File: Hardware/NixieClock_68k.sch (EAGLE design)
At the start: 56 parts, among them IC1 68008, IC10 7805, IC11 MIC803, IC12 74HC08N, IC2 AS6C1008, IC3 39SF020, IC4 DS1244Y, IC5 68681, IC6 74HC30N, IC7 74HC04N, IC8 74HC138N, IC9 74HC266N, Q1 4MHz, Q2 3.6864MHz

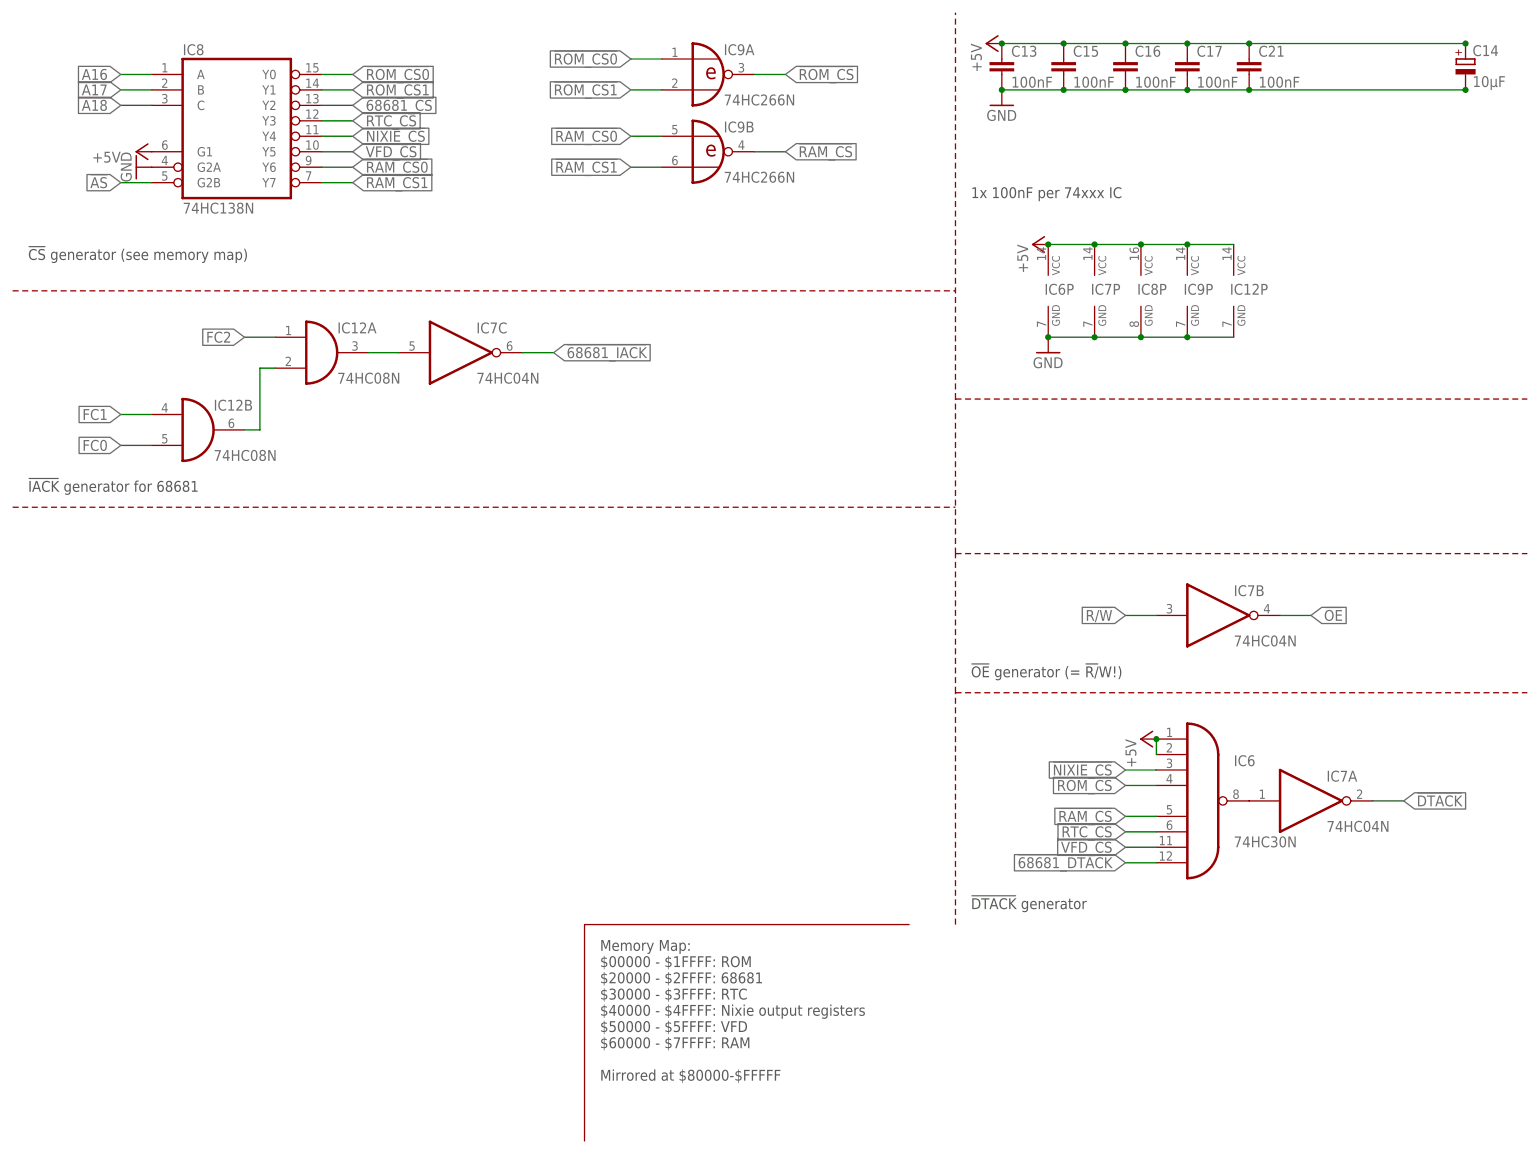
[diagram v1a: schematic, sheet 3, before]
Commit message: routed most system control signals
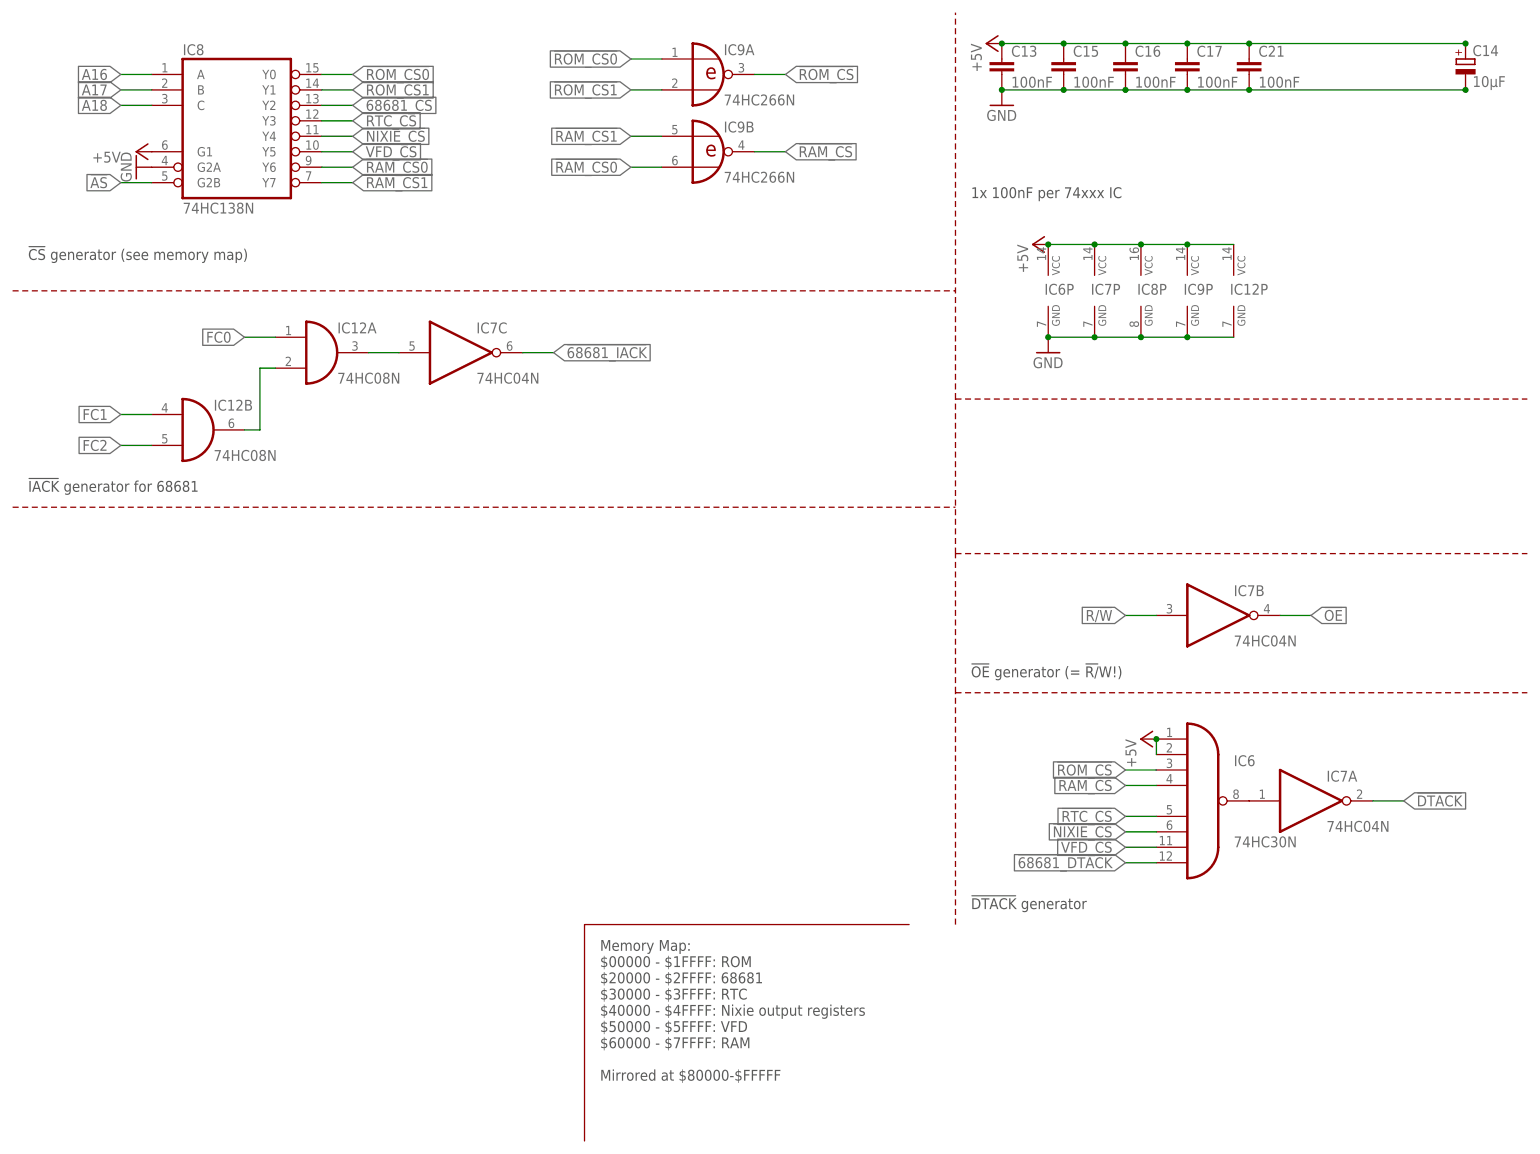
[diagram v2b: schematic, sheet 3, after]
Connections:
- net !NIXIE_CS: now also IC6A.I5; no longer IC6A.I2
- net !RAM_CS: now also IC6A.I3; no longer IC6A.I4
- net !RAM_CS0: now also IC9B.I1; no longer IC9B.I0
- net !RAM_CS1: now also IC9B.I0; no longer IC9B.I1
- net !ROM_CS: now also IC6A.I2; no longer IC6A.I3
- net !RTC_CS: now also IC6A.I4; no longer IC6A.I5
- net FC0: now also IC12A.I0; no longer IC12B.I1
- net FC2: now also IC12B.I1; no longer IC12A.I0
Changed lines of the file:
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@@
 <net name="!RTC_CS" class="0">
+<segment>
+<pinref part="IC8" gate="A" pin="Y3"/>
+<wire x1="50.8" y1="167.64" x2="55.88" y2="167.64" width="0.1524" layer="91"/>
+<label x="55.88" y="167.64" size="1.778" layer="95" xref="yes"/>
+</segment>
+<segment>
+<pinref part="IC6" gate="A" pin="I4"/>
+<wire x1="187.96" y1="53.34" x2="182.88" y2="53.34" width="0.1524" layer="91"/>
+<label x="182.88" y="53.34" size="1.778" layer="95" rot="R180" xref="yes"/>
+</segment>
+</net>
+<net name="!RAM_CS" class="0">
+<segment>
+<pinref part="IC9" gate="B" pin="O"/>
+<wire x1="121.92" y1="162.56" x2="127" y2="162.56" width="0.1524" layer="91"/>
+<label x="127" y="162.56" size="1.778" layer="95" xref="yes"/>
+</segment>
+<segment>
+<pinref part="IC6" gate="A" pin="I3"/>
+<wire x1="187.96" y1="58.42" x2="182.88" y2="58.42" width="0.1524" layer="91"/>
+<label x="182.88" y="58.42" size="1.778" layer="95" rot="R180" xref="yes"/>
+</segment>
+</net>
+<net name="!ROM_CS" class="0">
+<segment>
+<pinref part="IC9" gate="A" pin="O"/>
+<wire x1="121.92" y1="175.26" x2="127" y2="175.26" width="0.1524" layer="91"/>
+<label x="127" y="175.26" size="1.778" layer="95" xref="yes"/>
+</segment>
+<segment>
+<pinref part="IC6" gate="A" pin="I2"/>
+<wire x1="187.96" y1="60.96" x2="182.88" y2="60.96" width="0.1524" layer="91"/>
+<label x="182.88" y="60.96" size="1.778" layer="95" rot="R180" xref="yes"/>
+</segment>
+</net>
+<net name="!NIXIE_CS" class="0">
+<segment>
+<pinref part="IC8" gate="A" pin="Y4"/>
+<wire x1="50.8" y1="165.1" x2="55.88" y2="165.1" width="0.1524" layer="91"/>
+<label x="55.88" y="165.1" size="1.778" layer="95" xref="yes"/>
+</segment>
 <segment>
 <pinref part="IC6" gate="A" pin="I5"/>
@@
 <label x="182.88" y="50.8" size="1.778" layer="95" rot="R180" xref="yes"/>
 </segment>
-<segment>
-<pinref part="IC8" gate="A" pin="Y3"/>
-<wire x1="50.8" y1="167.64" x2="55.88" y2="167.64" width="0.1524" layer="91"/>
-<label x="55.88" y="167.64" size="1.778" layer="95" xref="yes"/>
-</segment>
-</net>
-<net name="!RAM_CS" class="0">
-<segment>
-<pinref part="IC6" gate="A" pin="I4"/>
-<wire x1="187.96" y1="53.34" x2="182.88" y2="53.34" width="0.1524" layer="91"/>
-<label x="182.88" y="53.34" size="1.778" layer="95" rot="R180" xref="yes"/>
-</segment>
-<segment>
-<pinref part="IC9" gate="B" pin="O"/>
-<wire x1="121.92" y1="162.56" x2="127" y2="162.56" width="0.1524" layer="91"/>
-<label x="127" y="162.56" size="1.778" layer="95" xref="yes"/>
-</segment>
-</net>
-<net name="!ROM_CS" class="0">
-<segment>
-<pinref part="IC6" gate="A" pin="I3"/>
-<wire x1="187.96" y1="58.42" x2="182.88" y2="58.42" width="0.1524" layer="91"/>
-<label x="182.88" y="58.42" size="1.778" layer="95" rot="R180" xref="yes"/>
-</segment>
-<segment>
-<pinref part="IC9" gate="A" pin="O"/>
-<wire x1="121.92" y1="175.26" x2="127" y2="175.26" width="0.1524" layer="91"/>
-<label x="127" y="175.26" size="1.778" layer="95" xref="yes"/>
-</segment>
-</net>
-<net name="!NIXIE_CS" class="0">
-<segment>
-<pinref part="IC6" gate="A" pin="I2"/>
-<wire x1="187.96" y1="60.96" x2="182.88" y2="60.96" width="0.1524" layer="91"/>
-<label x="182.88" y="60.96" size="1.778" layer="95" rot="R180" xref="yes"/>
-</segment>
-<segment>
-<pinref part="IC8" gate="A" pin="Y4"/>
-<wire x1="50.8" y1="165.1" x2="55.88" y2="165.1" width="0.1524" layer="91"/>
-<label x="55.88" y="165.1" size="1.778" layer="95" xref="yes"/>
-</segment>
 </net>
 <net name="A18" class="0">
@@
 </segment>
 <segment>
+<pinref part="IC9" gate="B" pin="I1"/>
+<wire x1="106.68" y1="160.02" x2="101.6" y2="160.02" width="0.1524" layer="91"/>
+<label x="101.6" y="160.02" size="1.778" layer="95" rot="R180" xref="yes"/>
+</segment>
+</net>
+<net name="!RAM_CS1" class="0">
+<segment>
+<pinref part="IC8" gate="A" pin="Y7"/>
+<wire x1="50.8" y1="157.48" x2="55.88" y2="157.48" width="0.1524" layer="91"/>
+<label x="55.88" y="157.48" size="1.778" layer="95" xref="yes"/>
+</segment>
+<segment>
 <pinref part="IC9" gate="B" pin="I0"/>
 <wire x1="106.68" y1="165.1" x2="101.6" y2="165.1" width="0.1524" layer="91"/>
@@
 </segment>
 </net>
-<net name="!RAM_CS1" class="0">
-<segment>
-<pinref part="IC8" gate="A" pin="Y7"/>
-<wire x1="50.8" y1="157.48" x2="55.88" y2="157.48" width="0.1524" layer="91"/>
-<label x="55.88" y="157.48" size="1.778" layer="95" xref="yes"/>
-</segment>
-<segment>
-<pinref part="IC9" gate="B" pin="I1"/>
-<wire x1="106.68" y1="160.02" x2="101.6" y2="160.02" width="0.1524" layer="91"/>
-<label x="101.6" y="160.02" size="1.778" layer="95" rot="R180" xref="yes"/>
-</segment>
-</net>
 <net name="!ROM_CS0" class="0">
 <segment>
@@
 <wire x1="58.42" y1="129.54" x2="63.5" y2="129.54" width="0.1524" layer="91"/>
 <pinref part="IC7" gate="C" pin="I"/>
-</segment>
-</net>
-<net name="FC2" class="0">
-<segment>
-<pinref part="IC12" gate="A" pin="I0"/>
-<wire x1="43.18" y1="132.08" x2="38.1" y2="132.08" width="0.1524" layer="91"/>
-<label x="38.1" y="132.08" size="1.778" layer="95" rot="R180" xref="yes"/>
 </segment>
 </net>
@@
 <net name="FC0" class="0">
 <segment>
+<pinref part="IC12" gate="A" pin="I0"/>
+<wire x1="43.18" y1="132.08" x2="38.1" y2="132.08" width="0.1524" layer="91"/>
+<label x="38.1" y="132.08" size="1.778" layer="95" rot="R180" xref="yes"/>
+</segment>
+</net>
+<net name="!68681_IACK" class="0">
+<segment>
+<pinref part="IC7" gate="C" pin="O"/>
+<wire x1="83.82" y1="129.54" x2="88.9" y2="129.54" width="0.1524" layer="91"/>
+<label x="88.9" y="129.54" size="1.778" layer="95" xref="yes"/>
+</segment>
+</net>
+<net name="FC2" class="0">
+<segment>
 <pinref part="IC12" gate="B" pin="I1"/>
 <wire x1="22.86" y1="114.3" x2="17.78" y2="114.3" width="0.1524" layer="91"/>
@@
 </segment>
 </net>
-<net name="!68681_IACK" class="0">
-<segment>
-<pinref part="IC7" gate="C" pin="O"/>
-<wire x1="83.82" y1="129.54" x2="88.9" y2="129.54" width="0.1524" layer="91"/>
-<label x="88.9" y="129.54" size="1.778" layer="95" xref="yes"/>
-</segment>
-</net>

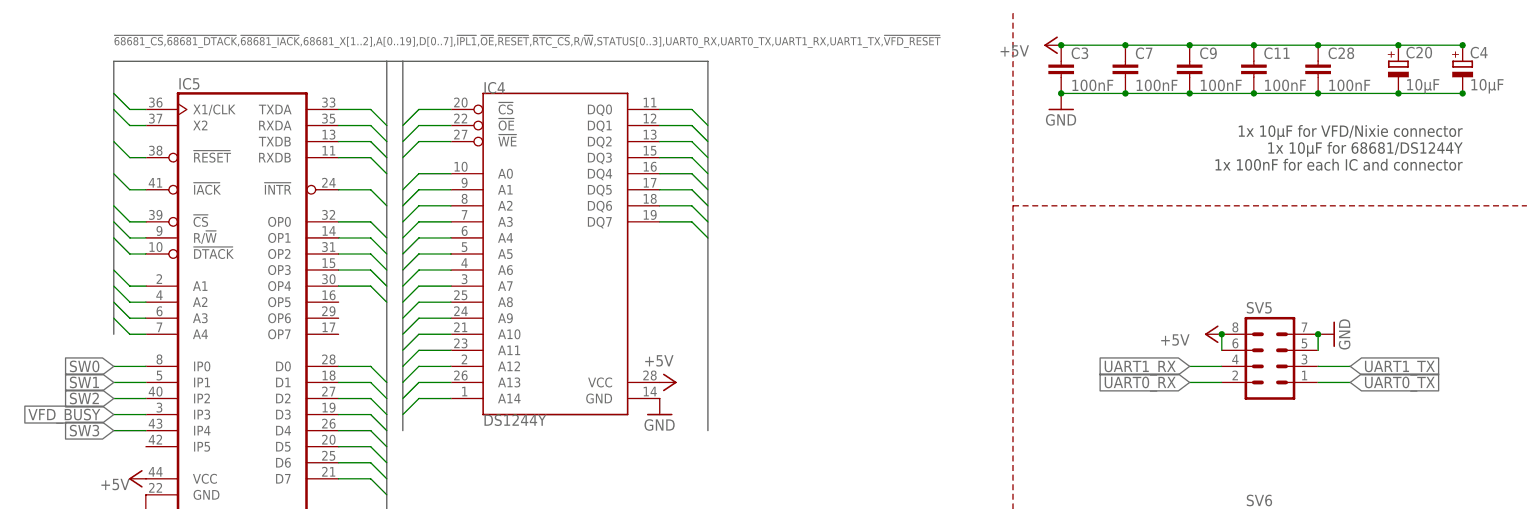
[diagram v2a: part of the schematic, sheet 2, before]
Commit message: routed 68681 data bus, some chip selects
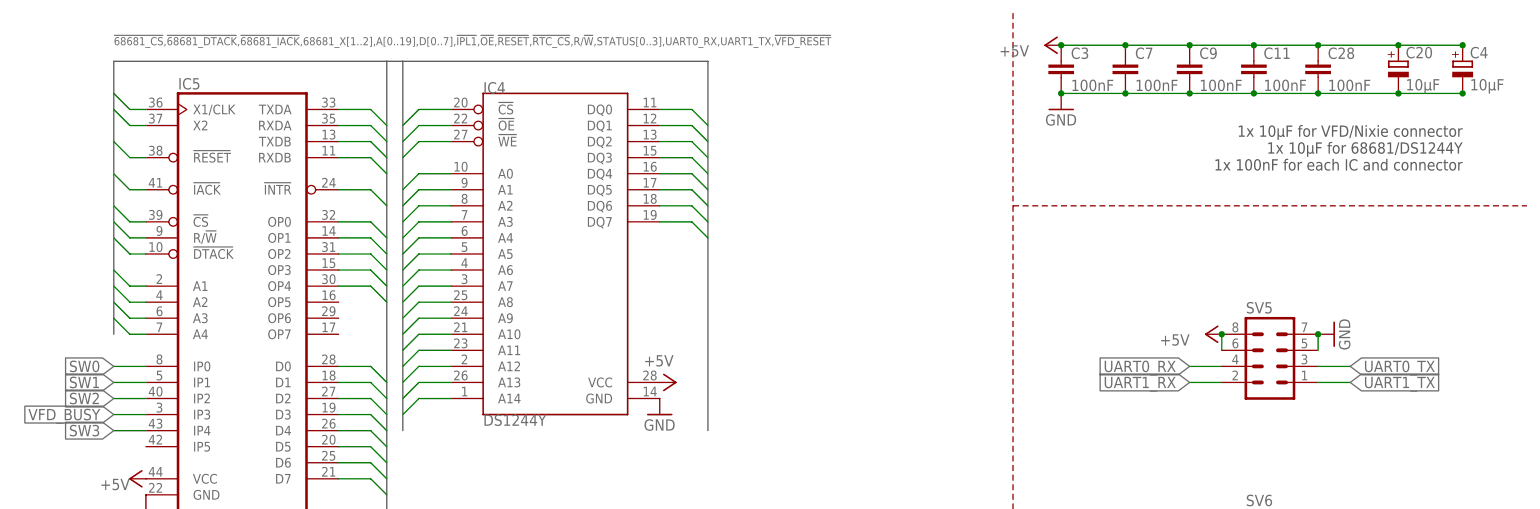
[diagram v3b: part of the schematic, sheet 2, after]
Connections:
- net UART0_RX: now also SV5.4; no longer SV5.2
- net UART0_TX: now also SV5.3; no longer SV5.1
- net UART1_RX: now also SV5.2; no longer SV5.4
- net UART1_TX: now also SV5.1; no longer SV5.3
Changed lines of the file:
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@@
 </instances>
 <busses>
-<bus name="!68681_CS,!68681_DTACK,!68681_IACK,68681_X[1..2],A[0..19],D[0..7],!IPL1,!OE,!RESET,!RTC_CS,R/!W!,STATUS[0..3],UART0_RX,UART0_TX,UART1_RX,UART1_TX,!VFD_RESET">
+<bus name="!68681_CS,!68681_DTACK,!68681_IACK,68681_X[1..2],A[0..19],D[0..7],!IPL1,!OE,!RESET,!RTC_CS,R/!W!,STATUS[0..3],UART0_RX,UART1_TX,!VFD_RESET">
 <segment>
 <wire x1="25.4" y1="177.8" x2="68.58" y2="177.8" width="0.762" layer="92"/>
@@
 </segment>
 <segment>
+<pinref part="SV5" gate="G$1" pin="3"/>
+<wire x1="215.9" y1="129.54" x2="220.98" y2="129.54" width="0.1524" layer="91"/>
+<label x="220.98" y="129.54" size="1.778" layer="95" xref="yes"/>
+</segment>
+</net>
+<net name="UART0_RX" class="0">
+<segment>
+<pinref part="IC5" gate="G$1" pin="RXDA"/>
+<wire x1="60.96" y1="167.64" x2="66.04" y2="167.64" width="0.1524" layer="91"/>
+<wire x1="66.04" y1="167.64" x2="68.58" y2="165.1" width="0.1524" layer="91"/>
+</segment>
+<segment>
+<pinref part="SV5" gate="G$1" pin="4"/>
+<wire x1="200.66" y1="129.54" x2="195.58" y2="129.54" width="0.1524" layer="91"/>
+<label x="195.58" y="129.54" size="1.778" layer="95" rot="R180" xref="yes"/>
+</segment>
+</net>
+<net name="UART1_TX" class="0">
+<segment>
+<pinref part="IC5" gate="G$1" pin="TXDB"/>
+<wire x1="60.96" y1="165.1" x2="66.04" y2="165.1" width="0.1524" layer="91"/>
+<wire x1="66.04" y1="165.1" x2="68.58" y2="162.56" width="0.1524" layer="91"/>
+</segment>
+<segment>
 <pinref part="SV5" gate="G$1" pin="1"/>
 <wire x1="215.9" y1="127" x2="220.98" y2="127" width="0.1524" layer="91"/>
@@
 </segment>
 </net>
-<net name="UART0_RX" class="0">
-<segment>
-<pinref part="IC5" gate="G$1" pin="RXDA"/>
-<wire x1="60.96" y1="167.64" x2="66.04" y2="167.64" width="0.1524" layer="91"/>
-<wire x1="66.04" y1="167.64" x2="68.58" y2="165.1" width="0.1524" layer="91"/>
+<net name="UART1_RX" class="0">
+<segment>
+<pinref part="IC5" gate="G$1" pin="RXDB"/>
+<wire x1="60.96" y1="162.56" x2="66.04" y2="162.56" width="0.1524" layer="91"/>
+<wire x1="66.04" y1="162.56" x2="68.58" y2="160.02" width="0.1524" layer="91"/>
 </segment>
 <segment>
@@
 </segment>
 </net>
-<net name="UART1_TX" class="0">
-<segment>
-<pinref part="IC5" gate="G$1" pin="TXDB"/>
-<wire x1="60.96" y1="165.1" x2="66.04" y2="165.1" width="0.1524" layer="91"/>
-<wire x1="66.04" y1="165.1" x2="68.58" y2="162.56" width="0.1524" layer="91"/>
-</segment>
-<segment>
-<pinref part="SV5" gate="G$1" pin="3"/>
-<wire x1="215.9" y1="129.54" x2="220.98" y2="129.54" width="0.1524" layer="91"/>
-<label x="220.98" y="129.54" size="1.778" layer="95" xref="yes"/>
-</segment>
-</net>
-<net name="UART1_RX" class="0">
-<segment>
-<pinref part="IC5" gate="G$1" pin="RXDB"/>
-<wire x1="60.96" y1="162.56" x2="66.04" y2="162.56" width="0.1524" layer="91"/>
-<wire x1="66.04" y1="162.56" x2="68.58" y2="160.02" width="0.1524" layer="91"/>
-</segment>
-<segment>
-<pinref part="SV5" gate="G$1" pin="4"/>
-<wire x1="200.66" y1="129.54" x2="195.58" y2="129.54" width="0.1524" layer="91"/>
-<label x="195.58" y="129.54" size="1.778" layer="95" rot="R180" xref="yes"/>
-</segment>
-</net>

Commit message: finished routing main board
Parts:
- removed C12, C18: 27pF, rcl:C-EUC0805
- removed C20: 10µF, rcl:CPOL-EUSMCB
- removed C21: 100nF, rcl:C-EUC0805
- removed LED6: (no value), led:LEDCHIPLED_1206
- removed Q2: 3.6864MHz, crystal:CRYSTALHC49S
- removed R1, R2: 100R, rcl:R-EU_R2012
- removed R19: 3k, rcl:R-EU_R2012
- Q1: value 4MHz -> 3.6864MHz; MOUSER 774-MXO45HS-3C-4.0 -> 774-MXO45HS-3C-3.6
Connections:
- removed net 68681_X1: IC5.X1/CLK, R2.1
- removed net 68681_X2: IC5.X2, R1.2
- removed net N$1: C12.1, Q2.2, R1.1
- removed net N$2: C18.1, Q2.1, R2.2
- removed net N$6: LED6.A, R19.2
- removed net STATUS2: IC5.OP2
- removed net STATUS3: IC5.OP3, R8.1
- removed net SW3: IC5.IP4, SV6.4
- net !RESET: no longer LED6.C
- net +5V: no longer C20.+, C21.1, R19.1, SV1.1
- net CLK: now also IC5.X1/CLK
- net GND: now also SV1.1; no longer C12.2, C18.2, C20.-, C21.2
- net STATUS0: now also IC5.OP7, R8.1; no longer IC5.OP0
- net STATUS1: now also IC5.OP5; no longer IC5.OP1
- net SW0: now also IC5.IP1; no longer IC5.IP0
- net SW1: now also IC5.IP0; no longer IC5.IP1
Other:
- note added: "1x 10µF for VFD/Nixie connector 1x 100nF for each IC and connector"
- note removed: "1x 10µF for VFD/Nixie connector 1x 10µF for 68681/DS1244Y 1x 100nF for each IC and connector"
